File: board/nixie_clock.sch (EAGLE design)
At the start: 39 parts, among them U1 AMS1117-5.0, U2 SN74141N

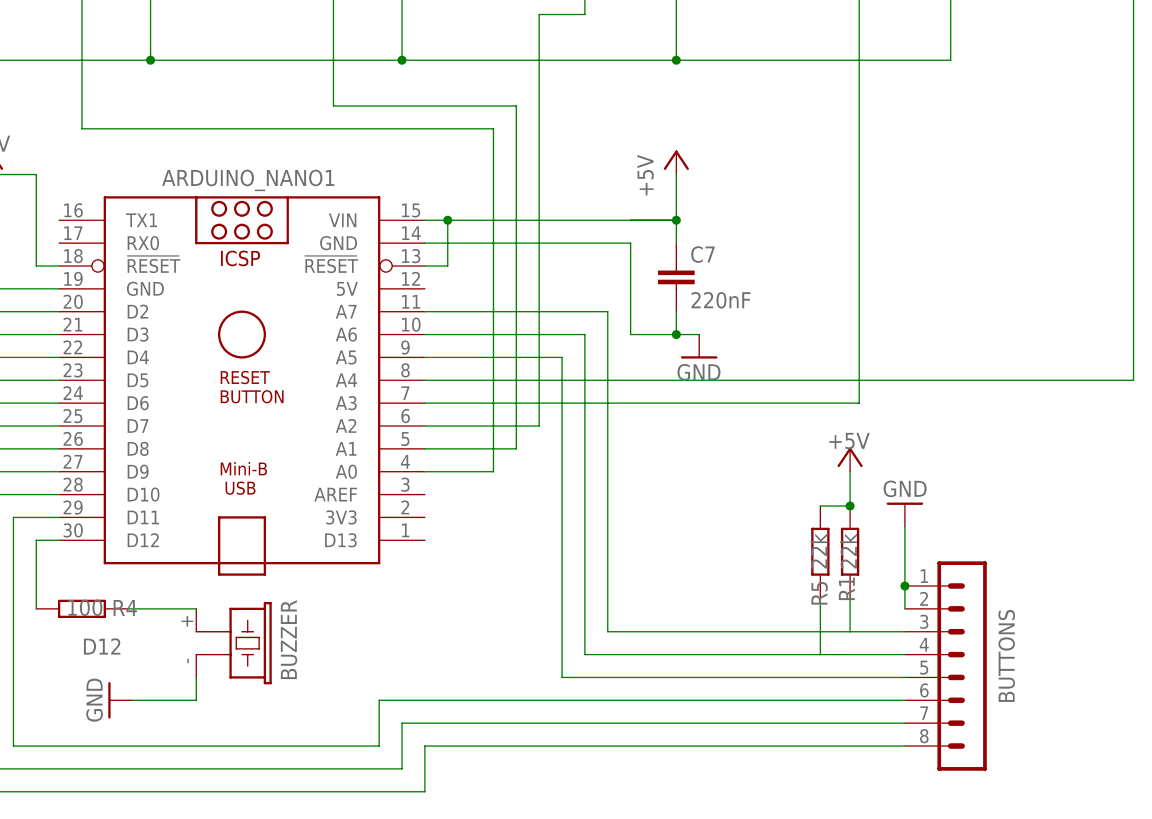
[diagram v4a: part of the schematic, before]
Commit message: D13 pin added and minor placement changes
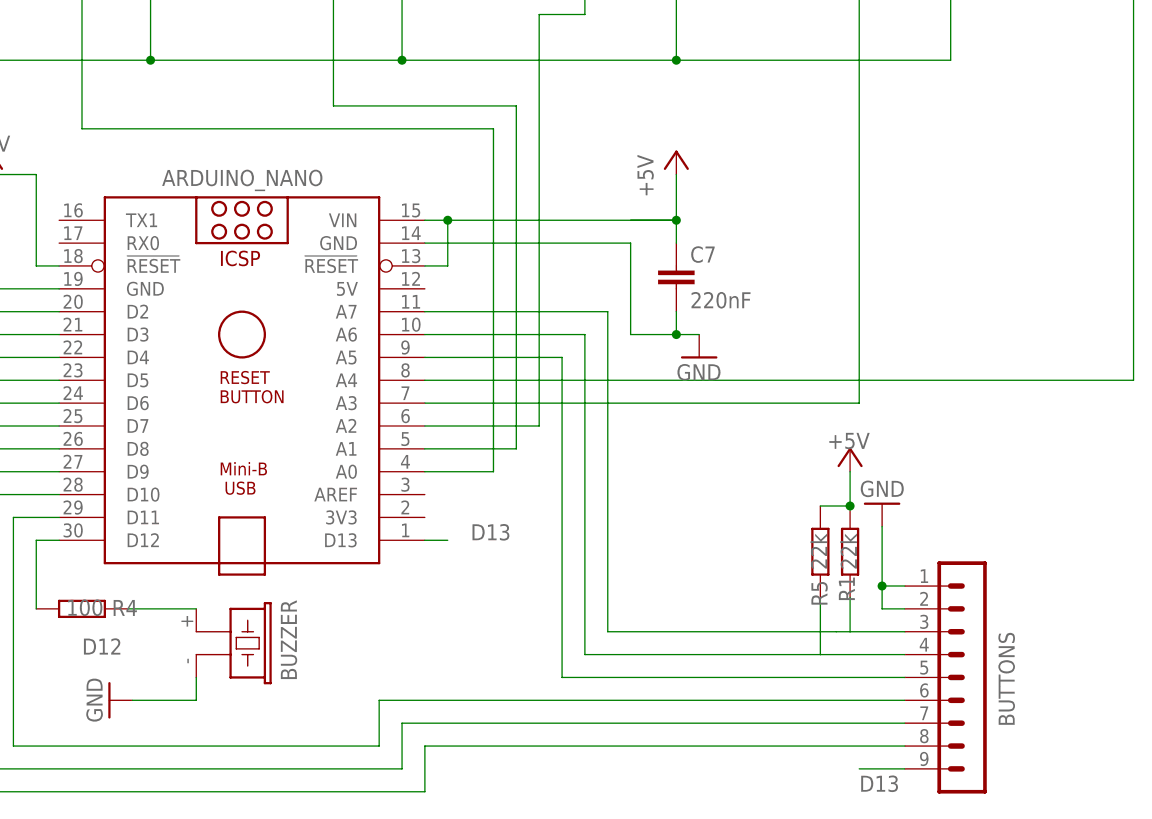
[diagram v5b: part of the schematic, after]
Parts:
- BUTTONS: device con-lstb:MA08-1 -> con-lstb:MA09-1
- renumbered ARDUINO_NANO1 to ARDUINO_NANO
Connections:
- new net D13: ARDUINO_NANO.D13, BUTTONS.9

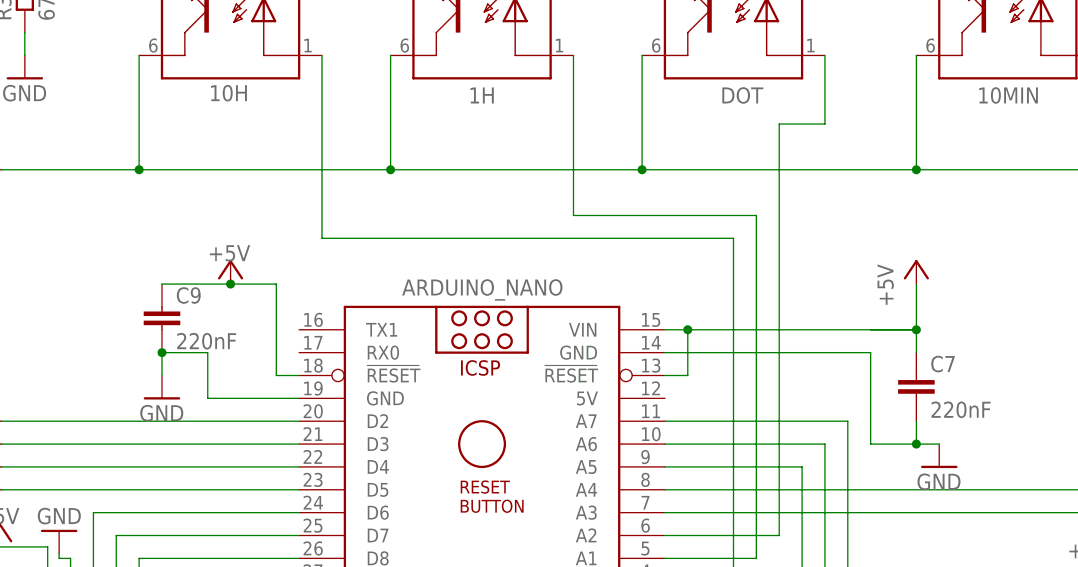
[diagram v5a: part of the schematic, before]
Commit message: Diode before Arduino's VIN added
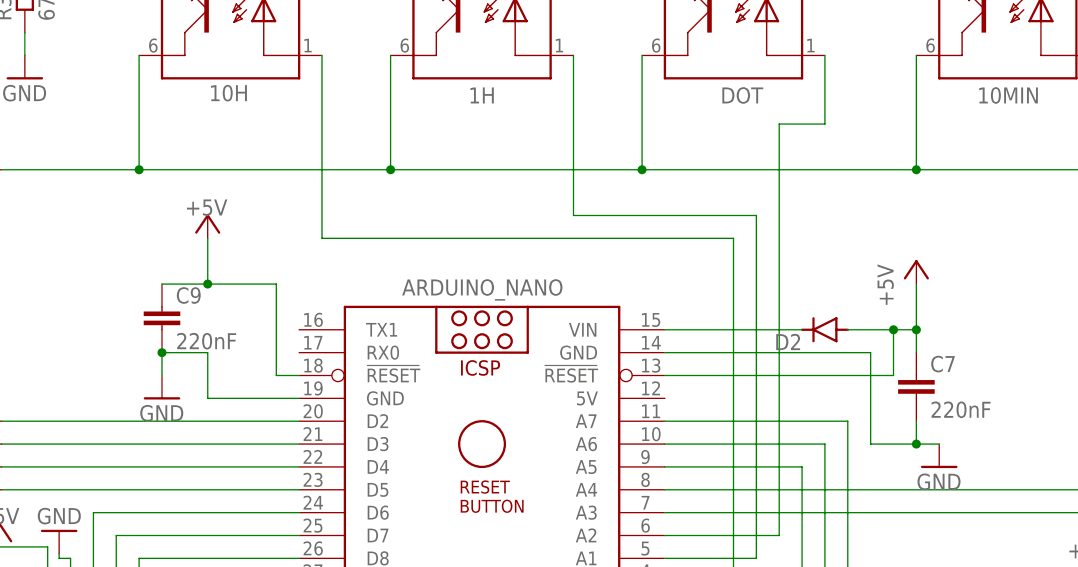
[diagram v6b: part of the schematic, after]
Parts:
- added D2: 1N4148DO35-7, diode:1N4148DO35-7
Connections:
- new net N$1: ARDUINO_NANO.VIN, D2.C
- net +5V: now also D2.A; no longer ARDUINO_NANO.VIN
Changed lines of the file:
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@@
 <part name="P+8" library="supply1" library_urn="urn:adsk.eagle:library:371" deviceset="+5V" device=""/>
 <part name="GND7" library="supply1" library_urn="urn:adsk.eagle:library:371" deviceset="GND" device=""/>
-<part name="P+9" library="supply1" library_urn="urn:adsk.eagle:library:371" deviceset="+5V" device=""/>
 <part name="GND2" library="supply1" library_urn="urn:adsk.eagle:library:371" deviceset="GND" device=""/>
 <part name="C7" library="capacitor-wima" library_urn="urn:adsk.eagle:library:116" deviceset="C" device="2,5-3" package3d_urn="urn:adsk.eagle:package:5436/1" value="220nF"/>
@@
 <part name="R1" library="rcl" library_urn="urn:adsk.eagle:library:334" deviceset="R-EU_" device="0204/7" package3d_urn="urn:adsk.eagle:package:23498/2" value="22k"/>
 <part name="R5" library="rcl" library_urn="urn:adsk.eagle:library:334" deviceset="R-EU_" device="0204/7" package3d_urn="urn:adsk.eagle:package:23498/2" value="22k"/>
+<part name="P+10" library="supply1" library_urn="urn:adsk.eagle:library:371" deviceset="+5V" device=""/>
+<part name="D2" library="diode" library_urn="urn:adsk.eagle:library:210" deviceset="1N4148" device="DO35-7" package3d_urn="urn:adsk.eagle:package:43339/2"/>
 </parts>
 <sheets>
@@
 <attribute name="VALUE" x="312.42" y="106.68" size="1.778" layer="96"/>
 </instance>
-<instance part="P+9" gate="1" x="322.58" y="124.46" smashed="yes">
-<attribute name="VALUE" x="320.04" y="124.46" size="1.778" layer="96"/>
-</instance>
 <instance part="GND2" gate="1" x="335.788" y="63.5" smashed="yes" rot="R270">
 <attribute name="VALUE" x="333.248" y="66.04" size="1.778" layer="96" rot="R270"/>
@@
 <attribute name="NAME" x="415.5694" y="73.914" size="1.778" layer="95" rot="R90"/>
 <attribute name="VALUE" x="415.544" y="77.978" size="1.778" layer="96" rot="R90"/>
+</instance>
+<instance part="P+10" gate="1" x="320.04" y="129.54" smashed="yes">
+<attribute name="VALUE" x="317.5" y="129.54" size="1.778" layer="96"/>
+</instance>
+<instance part="D2" gate="G$1" x="388.62" y="116.84" smashed="yes" rot="R180">
+<attribute name="NAME" x="386.08" y="116.3574" size="1.778" layer="95" rot="R180"/>
 </instance>
 </instances>
@@
 </segment>
 <segment>
-<pinref part="P+9" gate="1" pin="+5V"/>
 <pinref part="ARDUINO_NANO" gate="G$1" pin="!RESET@1"/>
-<wire x1="322.58" y1="121.92" x2="327.66" y2="121.92" width="0.1524" layer="91"/>
 <wire x1="327.66" y1="121.92" x2="327.66" y2="111.76" width="0.1524" layer="91"/>
 <wire x1="327.66" y1="111.76" x2="330.2" y2="111.76" width="0.1524" layer="91"/>
 <pinref part="C9" gate="G$1" pin="1"/>
-<wire x1="314.96" y1="121.92" x2="322.58" y2="121.92" width="0.1524" layer="91"/>
-<junction x="322.58" y="121.92"/>
+<wire x1="314.96" y1="121.92" x2="320.04" y2="121.92" width="0.1524" layer="91"/>
+<pinref part="P+10" gate="1" pin="+5V"/>
+<wire x1="320.04" y1="121.92" x2="327.66" y2="121.92" width="0.1524" layer="91"/>
+<wire x1="320.04" y1="127" x2="320.04" y2="121.92" width="0.1524" layer="91"/>
+<junction x="320.04" y="121.92"/>
 </segment>
 <segment>
@@
 </segment>
 <segment>
-<pinref part="ARDUINO_NANO" gate="G$1" pin="VIN"/>
-<pinref part="ARDUINO_NANO" gate="G$1" pin="!RESET@2"/>
-<wire x1="373.38" y1="116.84" x2="370.84" y2="116.84" width="0.1524" layer="91"/>
-<wire x1="370.84" y1="111.76" x2="373.38" y2="111.76" width="0.1524" layer="91"/>
-<wire x1="373.38" y1="111.76" x2="373.38" y2="116.84" width="0.1524" layer="91"/>
-<junction x="373.38" y="116.84"/>
-<wire x1="373.38" y1="116.84" x2="398.78" y2="116.84" width="0.1524" layer="91"/>
-<wire x1="398.78" y1="116.84" x2="393.7" y2="116.84" width="0.1524" layer="91"/>
+<wire x1="398.78" y1="116.84" x2="396.24" y2="116.84" width="0.1524" layer="91"/>
 <pinref part="C7" gate="G$1" pin="1"/>
+<wire x1="396.24" y1="116.84" x2="391.16" y2="116.84" width="0.1524" layer="91"/>
 <wire x1="398.78" y1="114.3" x2="398.78" y2="116.84" width="0.1524" layer="91"/>
 <junction x="398.78" y="116.84"/>
 <pinref part="P+8" gate="1" pin="+5V"/>
 <wire x1="398.78" y1="116.84" x2="398.78" y2="121.92" width="0.1524" layer="91"/>
+<pinref part="D2" gate="G$1" pin="A"/>
+<pinref part="ARDUINO_NANO" gate="G$1" pin="!RESET@2"/>
+<wire x1="370.84" y1="111.76" x2="396.24" y2="111.76" width="0.1524" layer="91"/>
+<wire x1="396.24" y1="111.76" x2="396.24" y2="116.84" width="0.1524" layer="91"/>
+<junction x="396.24" y="116.84"/>
 </segment>
 <segment>
@@
 </segment>
 </net>
+<net name="N$1" class="1">
+<segment>
+<pinref part="ARDUINO_NANO" gate="G$1" pin="VIN"/>
+<pinref part="D2" gate="G$1" pin="C"/>
+<wire x1="386.08" y1="116.84" x2="370.84" y2="116.84" width="0.1524" layer="91"/>
+</segment>
+</net>

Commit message: board design v3
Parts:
- removed RTC: (no value), con-lstb:MA05-1
- added Q1: BC546B, transistor-npn:BC546B
- added SV1: (no value), con-lstb:MA04-1
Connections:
- removed net D12: BUZZER.1, R4.2
- removed net N$17: ARDUINO_NANO.A5, BUTTONS.5
- removed net N$29: 1MIN.A, ARDUINO_NANO.A4
- removed net N$8: ARDUINO_NANO.D12, R4.1
- new net BUZ_IN: BUZZER.1, Q1.E
- new net BUZ_SGN: ARDUINO_NANO.D12, Q1.B
- new net SCL: ARDUINO_NANO.A5, SV1.1
- new net SDA: ARDUINO_NANO.A4, SV1.2
- net +5V: now also SV1.3; no longer RTC.5
- net GND: now also SV1.4; no longer RTC.4
- net N$3: now also 1MIN.A, ARDUINO_NANO.D6; no longer ARDUINO_NANO.D8, RTC.1
- net N$4: now also BUTTONS.5; no longer RTC.2
- net N$7: now also Q1.C, R4.2; no longer ARDUINO_NANO.D6, RTC.3
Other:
- moved on the sheet: BUZZER, R4

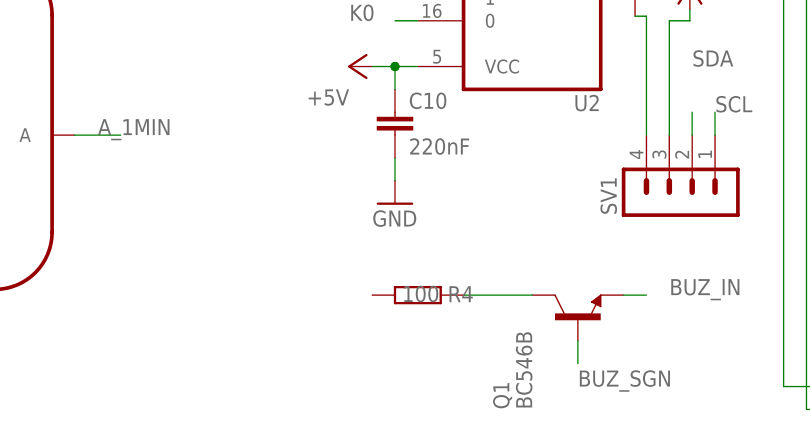
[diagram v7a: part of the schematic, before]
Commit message: Connected 12V to buzzer.
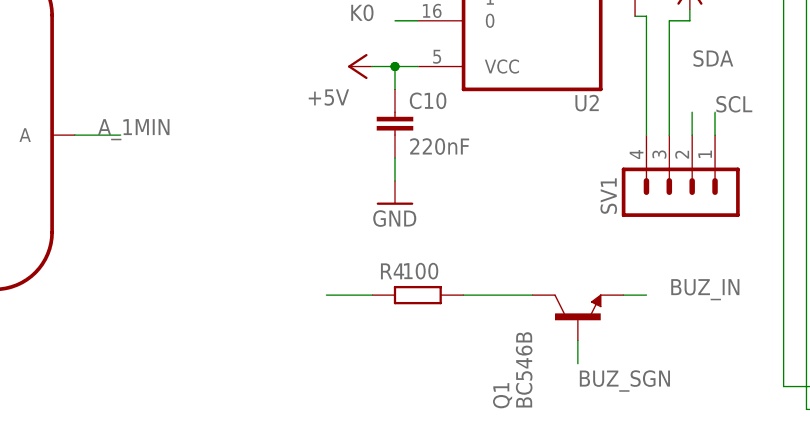
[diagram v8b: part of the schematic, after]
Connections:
- net +12V: now also R4.1
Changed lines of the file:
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@@
 </instance>
 <instance part="R4" gate="G$1" x="271.78" y="60.96" smashed="yes">
-<attribute name="NAME" x="275.082" y="60.1726" size="1.778" layer="95"/>
-<attribute name="VALUE" x="270.002" y="60.198" size="1.778" layer="96"/>
+<attribute name="NAME" x="267.462" y="62.7126" size="1.778" layer="95"/>
+<attribute name="VALUE" x="270.002" y="62.738" size="1.778" layer="96"/>
 </instance>
 <instance part="R10" gate="G$1" x="271.78" y="172.72" smashed="yes" rot="R90">
@@
 <junction x="226.06" y="152.4"/>
 </segment>
+<segment>
+<pinref part="R4" gate="G$1" pin="1"/>
+<wire x1="266.7" y1="60.96" x2="261.62" y2="60.96" width="0.1524" layer="91"/>
+</segment>
 </net>
